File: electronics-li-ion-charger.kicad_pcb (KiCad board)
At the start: 2 copper layers, 19.1 x 25.4 mm, 20 parts, among them J1 Conn_01x01_Male, J2 Conn_01x01_Male, J3 USB_B_Micro, J4 Conn_01x03_Male, M1 MountingHole_2.2mm_M2_Pad, M2 MountingHole_2.2mm_M2_Pad, M3 MountingHole_2.2mm_M2_Pad, M4 MountingHole_2.2mm_M2_Pad, U1 MCP73831-2-OT

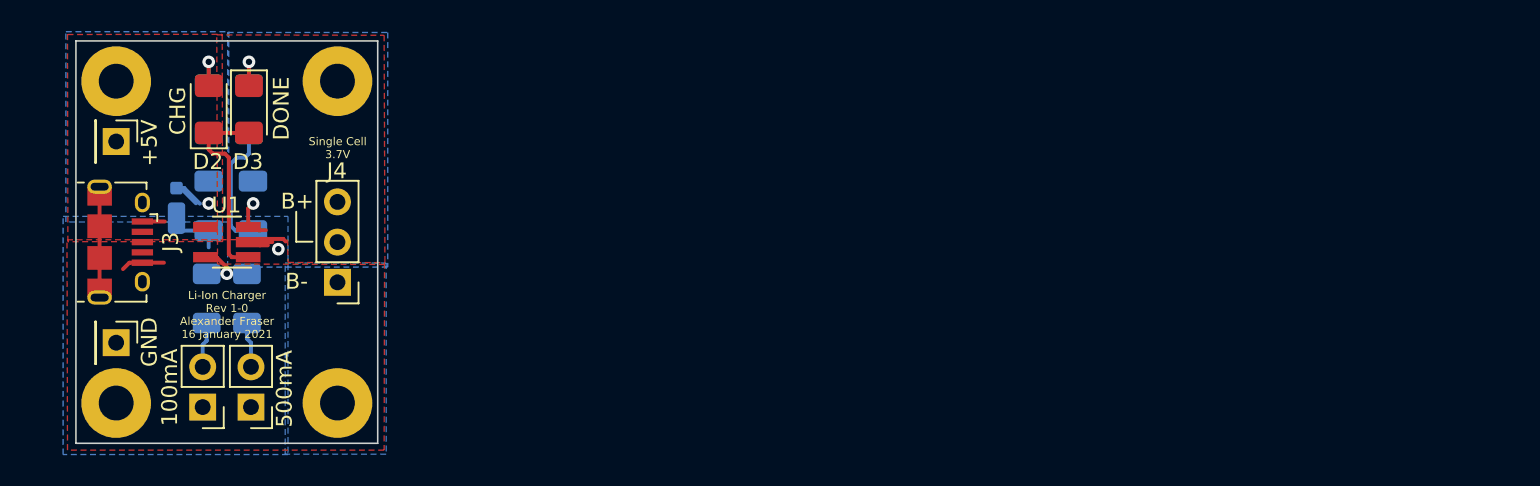
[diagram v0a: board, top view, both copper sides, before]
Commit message: Layout PCB with 18650 battery holder.
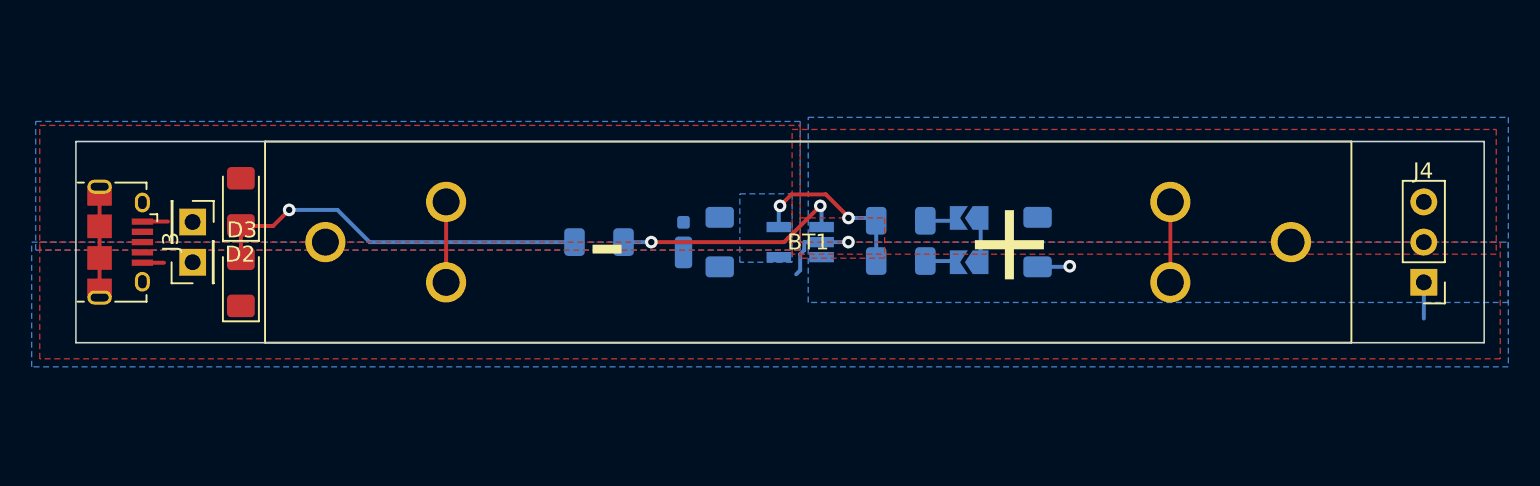
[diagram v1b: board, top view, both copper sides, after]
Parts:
- removed M1, M2, M3, M4: MountingHole_2.2mm_M2_Pad, MountingHole:MountingHole_2.2mm_M2_Pad
- removed R4: 470R, Resistor_SMD:R_1206_3216Metric_Pad1.30x1.75mm_HandSolder
- added BT1: Battery_Holder, electronics-li-ion-charger:Battery_Holder-PC_Pin-18650, F.Cu at (173.2, 101.6)
- JP1, JP2: footprint Connector_PinHeader_2.54mm:PinHeader_1x02_P2.54mm_Vertical -> Jumper:SolderJumper-2_P1.3mm_Open_TrianglePad1.0x1.5mm; moved to B.Cu
- U1: moved to B.Cu
- moved J4 68.6 mm to (212.1, 104.1)
- moved C2 49.6 mm to (187.7, 101.6)
- moved JP2 49.2 mm to (183.4, 102.9)
- moved JP1 46.9 mm to (183.4, 100.1)
- moved R2 43.9 mm to (179.1, 102.8), turned to 0 degrees
- moved R1 41.6 mm to (179.1, 100.3), turned to 0 degrees
- moved U1 36.2 mm to (172.7, 101.6)
- moved C1 32.3 mm to (167.6, 101.6)
- moved D1 32.1 mm to (165.4, 101.6)
- moved R3 26.0 mm to (160.0, 101.6), turned to 180 degrees
- moved D3 10.9 mm to (137.4, 104.1), turned to 90 degrees
- moved J1 7.01 mm to (134.4, 100.3)
- moved J2 7.01 mm to (134.4, 102.9), turned to 90 degrees
- moved D2 6.19 mm to (137.4, 99.1)
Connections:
- D2 pad 1: STAT -> Net-(D2-Pad1)
- D2 pad 2: Net-(D2-Pad2) -> +5V
- D3 pad 1: Net-(D3-Pad1) -> GND
- D3 pad 2: STAT -> Net-(D2-Pad1)
- R3 pad 1: +5V -> STAT
- R3 pad 2: Net-(D2-Pad2) -> Net-(D2-Pad1)
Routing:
- net Net-(D2-Pad1): track 0.00 -> 24.4 mm, vias 0 -> 1
- net PROG: track 7.88 -> 11.4 mm, vias 1 -> 2
- net +5V: track 4.92 -> 1.62 mm, vias 1 -> 0
- net Net-(D3-Pad1): track 3.11 -> 0.00 mm, vias 1 -> 0
- net Net-(D2-Pad2): track 2.96 -> 0.00 mm, vias 1 -> 0
- net STAT: track 12.5 -> 14.8 mm, vias 0 -> 2
- net /VBAT: track 2.82 -> 5.08 mm, vias 1 -> 0
- net GND: track 20.1 -> 18.6 mm, vias 1 -> 2
- net Net-(JP2-Pad2): track 2.87 -> 2.07 mm
- net Net-(JP1-Pad2): track 2.87 -> 2.12 mm
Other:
- board size 19.1 x 25.4 mm -> 88.9 x 12.7 mm
- board text removed: "+"
- board text removed: "+5V"
- board text removed: "-"
- board text removed: "100mA"
- board text removed: "500mA"
- board text removed: "B+"
- board text removed: "B-"
- board text removed: "CHG"
- board text removed: "DONE"
- board text removed: "GND"
- board text removed: "Li-Ion Charger Rev 1-0 Alexander Fraser 16 January 2021"
- board text removed: "Single Cell 3.7V"

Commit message: Modify layout with 18650 holder and fix silkscreen.
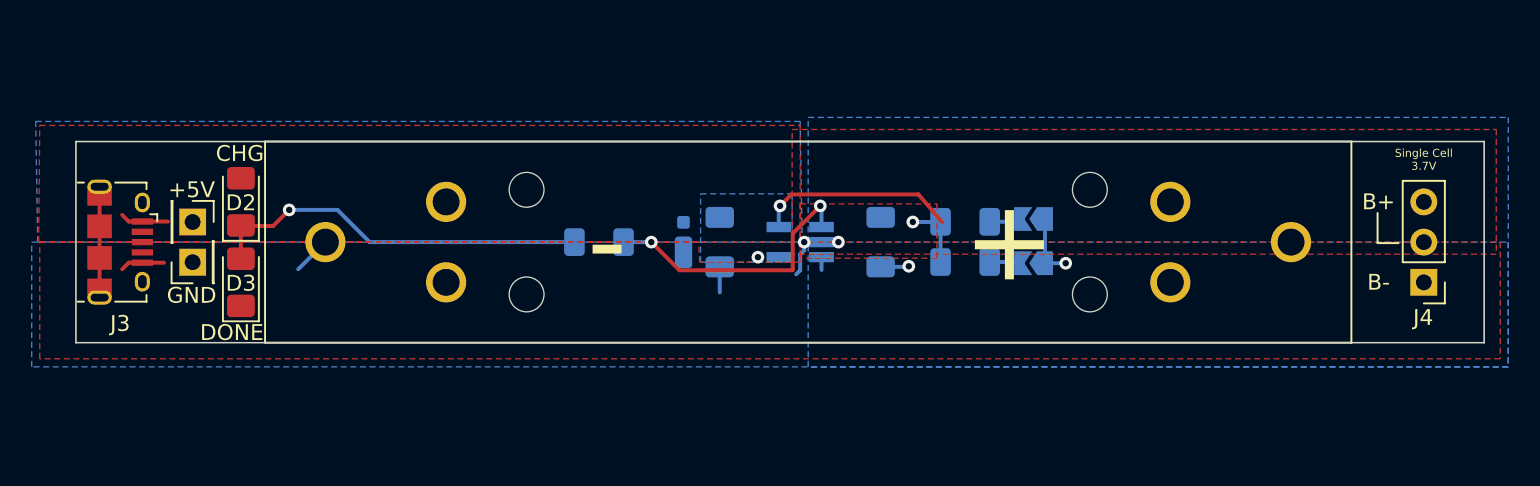
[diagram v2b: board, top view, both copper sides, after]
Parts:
- added M1: MountingHole_2.2mm_M2, MountingHole:MountingHole_2.2mm_M2, F.Cu at (155.4, 98.3)
- added M2: MountingHole_2.2mm_M2, MountingHole:MountingHole_2.2mm_M2, F.Cu at (155.4, 104.9)
- added M3: MountingHole_2.2mm_M2, MountingHole:MountingHole_2.2mm_M2, F.Cu at (191.0, 98.3)
- added M4: MountingHole_2.2mm_M2, MountingHole:MountingHole_2.2mm_M2, F.Cu at (191.0, 104.9)
- moved C2 9.91 mm to (177.8, 101.6)
- moved JP1 4.06 mm to (187.5, 100.1)
- moved JP2 4.06 mm to (187.5, 102.9)
- moved R1 4.06 mm to (183.1, 100.3)
- moved R2 4.06 mm to (183.1, 102.9)
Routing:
- net PROG: track 11.4 -> 17.6 mm
- net /VBAT: track 5.08 -> 0.81 mm
- net STAT: track 14.8 -> 17.7 mm
- net GND: track 18.6 -> 17.1 mm, vias 2 -> 4
- net +5V: track 1.62 -> 3.06 mm, vias 0 -> 1
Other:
- board text added: "+"
- board text added: "+5V"
- board text added: "-"
- board text added: "100mA"
- board text added: "500mA"
- board text added: "B+"
- board text added: "B-"
- board text added: "CHG"
- board text added: "DONE"
- board text added: "GND"
- board text added: "Li-Ion Charger Rev2-0 Alexander Fraser 17 January 2021"
- board text added: "Single Cell 3.7V"
